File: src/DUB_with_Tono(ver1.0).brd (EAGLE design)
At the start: 100 x 80 mm, 3 parts

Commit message: ベタの追加
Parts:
- removed EDGE1: 10046971-019LF, 10046971-019LF:10046971-019LF
- removed U$2: 5-5530843-4, 5-5530843-4:5-5530843-4
- added DUB: 10046971-019LF, 10046971-019LF:10046971-019LF
- added 遠野: 5-5530843-4, 5-5530843-4:5-5530843-4
- moved U$1 70.8 mm to (45.1, 8.33)
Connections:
- removed net N$1: U$2.P$1, U$2.P$2, U$2.P$3, U$2.P$37, U$2.P$38, U$2.P$39, U$2.P$4, U$2.P$40
- net DIR_IN: now also DUB.P$26, 遠野.P$21; no longer EDGE1.P$26
- net GND: now also DUB.P$28, DUB.P$29, DUB.P$30, DUB.P$31, DUB.P$32, DUB.P$33, DUB.P$34, DUB.P$35, DUB.P$36, DUB.P$37, DUB.P$38, DUB.P$39, 遠野.P$14, 遠野.P$15, 遠野.P$16, 遠野.P$17, 遠野.P$18, 遠野.P$23, 遠野.P$24, 遠野.P$25, 遠野.P$26, 遠野.P$27; no longer EDGE1.P$28, EDGE1.P$29, EDGE1.P$30, EDGE1.P$31, EDGE1.P$32, EDGE1.P$33, EDGE1.P$34, EDGE1.P$35, EDGE1.P$36, EDGE1.P$37, EDGE1.P$38, EDGE1.P$39
- net GND_IN: now also DUB.P$24, 遠野.P$19; no longer EDGE1.P$24
- net PWM_IN: now also DUB.P$25, 遠野.P$20; no longer EDGE1.P$25
- net SA: now also DUB.P$1, DUB.P$2, DUB.P$3, DUB.P$4, DUB.P$45, DUB.P$46, DUB.P$47, DUB.P$48, DUB.P$49, DUB.P$5, DUB.P$50, 遠野.P$1, 遠野.P$2, 遠野.P$3, 遠野.P$37, 遠野.P$38, 遠野.P$39, 遠野.P$4, 遠野.P$40; no longer EDGE1.P$1, EDGE1.P$2, EDGE1.P$3, EDGE1.P$4, EDGE1.P$45, EDGE1.P$46, EDGE1.P$47, EDGE1.P$48, EDGE1.P$49, EDGE1.P$5, EDGE1.P$50
- net SB: now also DUB.P$10, DUB.P$11, DUB.P$40, DUB.P$41, DUB.P$42, DUB.P$43, DUB.P$44, DUB.P$6, DUB.P$7, DUB.P$8, DUB.P$9, 遠野.P$33, 遠野.P$34, 遠野.P$35, 遠野.P$36, 遠野.P$5, 遠野.P$6, 遠野.P$7, 遠野.P$8; no longer EDGE1.P$10, EDGE1.P$11, EDGE1.P$40, EDGE1.P$41, EDGE1.P$42, EDGE1.P$43, EDGE1.P$44, EDGE1.P$6, EDGE1.P$7, EDGE1.P$8, EDGE1.P$9
- net VCC: now also DUB.P$12, DUB.P$13, DUB.P$14, DUB.P$15, DUB.P$16, DUB.P$17, DUB.P$18, DUB.P$19, DUB.P$20, DUB.P$21, DUB.P$22, DUB.P$23, 遠野.P$10, 遠野.P$11, 遠野.P$12, 遠野.P$13, 遠野.P$28, 遠野.P$29, 遠野.P$30, 遠野.P$31, 遠野.P$32, 遠野.P$9; no longer EDGE1.P$12, EDGE1.P$13, EDGE1.P$14, EDGE1.P$15, EDGE1.P$16, EDGE1.P$17, EDGE1.P$18, EDGE1.P$19, EDGE1.P$20, EDGE1.P$21, EDGE1.P$22, EDGE1.P$23
- net VCC_IN: now also DUB.P$27, 遠野.P$22; no longer EDGE1.P$27
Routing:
- net VCC_IN: track 0.00 -> 14.0 mm
- net GND_IN: track 0.00 -> 14.0 mm
- net DIR_IN: track 0.00 -> 14.0 mm
- net PWM_IN: track 0.00 -> 14.0 mm
- added copper zone on layer 1, net GND
- added copper zone on layer 16, net GND
- added copper zone on layer 1, net SA
- added copper zone on layer 16, net SA
- added copper zone on layer 1, net SB
- added copper zone on layer 16, net SB
- added copper zone on layer 1, net VCC
- added copper zone on layer 16, net VCC
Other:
- board size 100 x 80 mm -> 66 x 21.6 mm

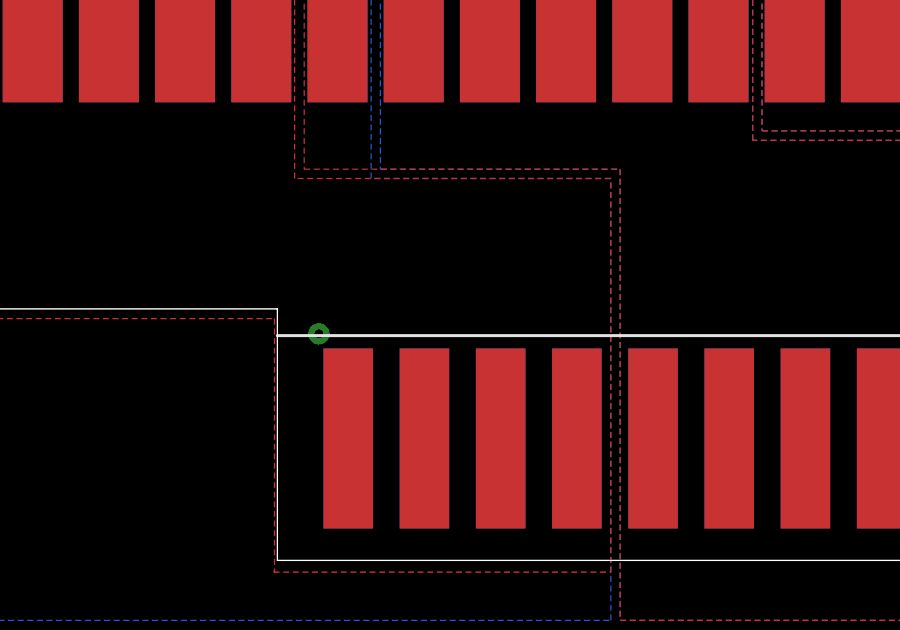
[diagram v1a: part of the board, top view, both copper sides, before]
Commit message: ビアの追加
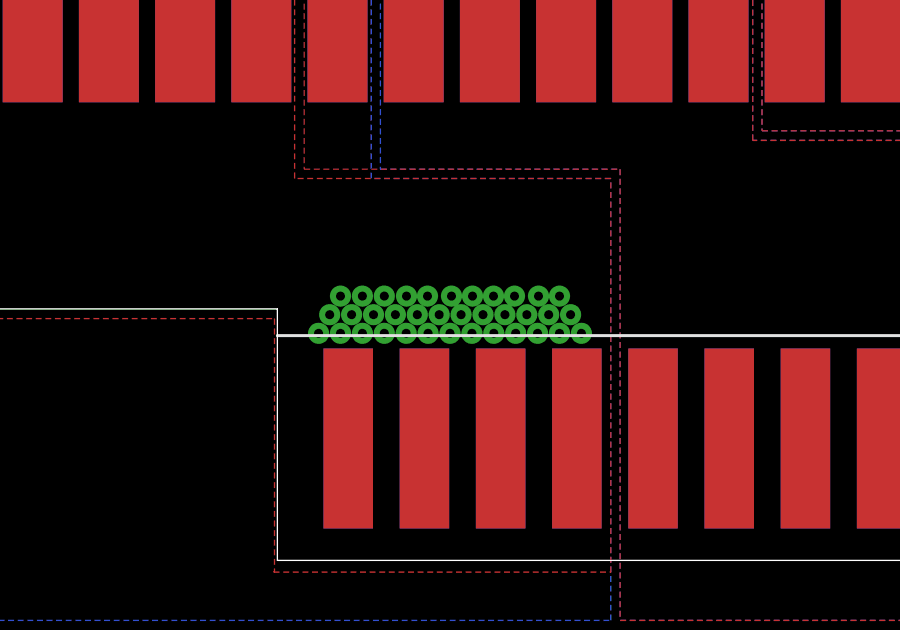
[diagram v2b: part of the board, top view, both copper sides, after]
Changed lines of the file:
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@@
 <setting verticaltext="up"/>
 </settings>
-<grid distance="0.01" unitdist="mm" unit="mm" style="lines" multiple="1" display="no" altdistance="0.01" altunitdist="mm" altunit="mm"/>
+<grid distance="0.1" unitdist="mm" unit="mm" style="lines" multiple="1" display="no" altdistance="0.01" altunitdist="mm" altunit="mm"/>
 <layers>
 <layer number="1" name="Top" color="4" fill="1" visible="yes" active="yes"/>
@@
 <vertex x="13.63" y="21.811109375"/>
 </polygon>
+<via x="14.43" y="7.57" extent="1-16" drill="0.3"/>
+<via x="14.8" y="8.19" extent="1-16" drill="0.3"/>
+<via x="15.16" y="8.81" extent="1-16" drill="0.3"/>
+<via x="15.16" y="7.57" extent="1-16" drill="0.3"/>
+<via x="15.53" y="8.19" extent="1-16" drill="0.3"/>
+<via x="15.89" y="8.81" extent="1-16" drill="0.3"/>
+<via x="15.89" y="7.57" extent="1-16" drill="0.3"/>
+<via x="16.26" y="8.19" extent="1-16" drill="0.3"/>
+<via x="16.62" y="8.81" extent="1-16" drill="0.3"/>
+<via x="16.62" y="7.57" extent="1-16" drill="0.3"/>
+<via x="16.99" y="8.19" extent="1-16" drill="0.3"/>
+<via x="17.36" y="8.81" extent="1-16" drill="0.3"/>
+<via x="17.35" y="7.57" extent="1-16" drill="0.3"/>
+<via x="17.72" y="8.19" extent="1-16" drill="0.3"/>
+<via x="18.06" y="8.81" extent="1-16" drill="0.3"/>
+<via x="18.08" y="7.57" extent="1-16" drill="0.3"/>
+<via x="18.45" y="8.19" extent="1-16" drill="0.3"/>
+<via x="18.86" y="8.81" extent="1-16" drill="0.3"/>
+<via x="18.81" y="7.57" extent="1-16" drill="0.3"/>
+<via x="19.54" y="7.57" extent="1-16" drill="0.3"/>
+<via x="20.27" y="7.57" extent="1-16" drill="0.3"/>
+<via x="21" y="7.57" extent="1-16" drill="0.3"/>
+<via x="21.73" y="7.57" extent="1-16" drill="0.3"/>
+<via x="22.46" y="7.57" extent="1-16" drill="0.3"/>
+<via x="23.19" y="7.57" extent="1-16" drill="0.3"/>
+<via x="19.18" y="8.19" extent="1-16" drill="0.3"/>
+<via x="19.91" y="8.19" extent="1-16" drill="0.3"/>
+<via x="20.64" y="8.19" extent="1-16" drill="0.3"/>
+<via x="21.37" y="8.19" extent="1-16" drill="0.3"/>
+<via x="22.1" y="8.19" extent="1-16" drill="0.3"/>
+<via x="22.83" y="8.19" extent="1-16" drill="0.3"/>
+<via x="19.56" y="8.81" extent="1-16" drill="0.3"/>
+<via x="20.26" y="8.81" extent="1-16" drill="0.3"/>
+<via x="20.96" y="8.81" extent="1-16" drill="0.3"/>
+<via x="21.76" y="8.81" extent="1-16" drill="0.3"/>
+<via x="22.46" y="8.81" extent="1-16" drill="0.3"/>
+<wire x1="12.52" y1="17.92" x2="15.06" y2="17.92" width="0" layer="19" extent="16-16"/>
+<wire x1="12.52" y1="17.92" x2="12.52" y2="17.92" width="0" layer="19" extent="1-16"/>
+<wire x1="9.98" y1="17.92" x2="12.52" y2="17.92" width="0" layer="19" extent="1-16"/>
+<wire x1="9.98" y1="17.92" x2="9.98" y2="17.92" width="0" layer="19" extent="1-16"/>
+<wire x1="7.44" y1="17.92" x2="9.98" y2="17.92" width="0" layer="19" extent="1-1"/>
+<wire x1="7.44" y1="17.92" x2="7.44" y2="17.92" width="0" layer="19" extent="1-16"/>
+<wire x1="4.9" y1="17.92" x2="7.44" y2="17.92" width="0" layer="19" extent="1-1"/>
+<wire x1="4.9" y1="17.92" x2="4.9" y2="17.92" width="0" layer="19" extent="1-16"/>
+<wire x1="2.36" y1="17.92" x2="4.9" y2="17.92" width="0" layer="19" extent="1-1"/>
+<wire x1="2.36" y1="17.92" x2="2.36" y2="17.92" width="0" layer="19" extent="1-16"/>
+<wire x1="15.16" y1="8.81" x2="15.06" y2="17.92" width="0" layer="19" extent="16-16"/>
+<wire x1="15.53" y1="8.19" x2="15.16" y2="8.81" width="0" layer="19" extent="1-1"/>
+<wire x1="15.89" y1="8.81" x2="15.16" y2="8.81" width="0" layer="19" extent="1-1"/>
+<wire x1="16.26" y1="8.19" x2="15.53" y2="8.19" width="0" layer="19" extent="1-1"/>
+<wire x1="16.62" y1="8.81" x2="15.89" y2="8.81" width="0" layer="19" extent="1-1"/>
+<wire x1="16.99" y1="8.19" x2="16.26" y2="8.19" width="0" layer="19" extent="1-1"/>
+<wire x1="17.36" y1="8.81" x2="16.62" y2="8.81" width="0" layer="19" extent="1-1"/>
+<wire x1="18.06" y1="8.81" x2="17.36" y2="8.81" width="0" layer="19" extent="1-1"/>
+<wire x1="17.72" y1="8.19" x2="18.06" y2="8.81" width="0" layer="19" extent="1-1"/>
+<wire x1="18.45" y1="8.19" x2="18.06" y2="8.81" width="0" layer="19" extent="1-1"/>
+<wire x1="19.18" y1="8.19" x2="18.45" y2="8.19" width="0" layer="19" extent="1-1"/>
+<wire x1="18.86" y1="8.81" x2="19.18" y2="8.19" width="0" layer="19" extent="1-1"/>
+<wire x1="19.56" y1="8.81" x2="18.86" y2="8.81" width="0" layer="19" extent="1-1"/>
+<wire x1="19.91" y1="8.19" x2="19.56" y2="8.81" width="0" layer="19" extent="1-1"/>
+<wire x1="20.26" y1="8.81" x2="19.56" y2="8.81" width="0" layer="19" extent="1-1"/>
+<wire x1="20.96" y1="8.81" x2="20.26" y2="8.81" width="0" layer="19" extent="1-1"/>
+<wire x1="20.64" y1="8.19" x2="20.96" y2="8.81" width="0" layer="19" extent="1-1"/>
+<wire x1="21.37" y1="8.19" x2="20.64" y2="8.19" width="0" layer="19" extent="1-1"/>
+<wire x1="22.1" y1="8.19" x2="21.37" y2="8.19" width="0" layer="19" extent="1-1"/>
+<wire x1="21.76" y1="8.81" x2="22.1" y2="8.19" width="0" layer="19" extent="1-1"/>
+<wire x1="22.46" y1="8.81" x2="21.76" y2="8.81" width="0" layer="19" extent="1-1"/>
+<wire x1="22.83" y1="8.19" x2="22.1" y2="8.19" width="0" layer="19" extent="1-1"/>
+<wire x1="23.19" y1="7.57" x2="22.83" y2="8.19" width="0" layer="19" extent="1-1"/>
+<wire x1="21" y1="7.57" x2="20.64" y2="8.19" width="0" layer="19" extent="1-1"/>
+<wire x1="21.73" y1="7.57" x2="21.37" y2="8.19" width="0" layer="19" extent="1-1"/>
+<wire x1="22.46" y1="7.57" x2="22.1" y2="8.19" width="0" layer="19" extent="1-1"/>
+<wire x1="18.08" y1="7.57" x2="17.72" y2="8.19" width="0" layer="19" extent="1-1"/>
+<wire x1="18.81" y1="7.57" x2="18.45" y2="8.19" width="0" layer="19" extent="1-1"/>
+<wire x1="19.54" y1="7.57" x2="19.18" y2="8.19" width="0" layer="19" extent="1-1"/>
+<wire x1="20.27" y1="7.57" x2="19.91" y2="8.19" width="0" layer="19" extent="1-1"/>
+<wire x1="14.8" y1="8.19" x2="15.16" y2="8.81" width="0" layer="19" extent="1-1"/>
+<wire x1="15.89" y1="7.57" x2="15.53" y2="8.19" width="0" layer="19" extent="1-1"/>
+<wire x1="16.62" y1="7.57" x2="16.26" y2="8.19" width="0" layer="19" extent="1-1"/>
+<wire x1="17.35" y1="7.57" x2="16.99" y2="8.19" width="0" layer="19" extent="1-1"/>
+<wire x1="14.43" y1="7.57" x2="14.8" y2="8.19" width="0" layer="19" extent="1-1"/>
+<wire x1="15.16" y1="7.57" x2="15.53" y2="8.19" width="0" layer="19" extent="1-1"/>
+<wire x1="23.0378" y1="4.064" x2="23.19" y2="7.57" width="0" layer="19" extent="1-1"/>
+<wire x1="23.0378" y1="4.064" x2="23.0378" y2="4.064" width="0" layer="19" extent="1-16"/>
+<wire x1="20.4978" y1="4.064" x2="23.0378" y2="4.064" width="0" layer="19" extent="1-1"/>
+<wire x1="20.4978" y1="4.064" x2="20.4978" y2="4.064" width="0" layer="19" extent="1-16"/>
+<wire x1="17.9578" y1="4.064" x2="20.4978" y2="4.064" width="0" layer="19" extent="1-1"/>
+<wire x1="17.9578" y1="4.064" x2="17.9578" y2="4.064" width="0" layer="19" extent="1-16"/>
+<wire x1="15.4178" y1="4.064" x2="17.9578" y2="4.064" width="0" layer="19" extent="1-1"/>
 <wire x1="15.4178" y1="4.064" x2="15.4178" y2="4.064" width="0" layer="19" extent="1-16"/>
 </signal>
@@
 <wire x1="35.7378" y1="4.064" x2="35.7378" y2="4.064" width="0" layer="19" extent="1-16"/>
 </signal>
-<signal name="N$2">
-<via x="14.44" y="7.55" extent="1-16" drill="0.3"/>
-</signal>
 </signals>

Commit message: 前バージョン
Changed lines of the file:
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@@
 <setting verticaltext="up"/>
 </settings>
-<grid distance="0.1" unitdist="mm" unit="mm" style="lines" multiple="1" display="no" altdistance="0.01" altunitdist="mm" altunit="mm"/>
+<grid distance="0.01" unitdist="mm" unit="mm" style="lines" multiple="1" display="no" altdistance="0.01" altunitdist="mm" altunit="mm"/>
 <layers>
 <layer number="1" name="Top" color="4" fill="1" visible="yes" active="yes"/>
@@
 <vertex x="13.63" y="21.811109375"/>
 </polygon>
-<via x="14.43" y="7.57" extent="1-16" drill="0.3"/>
-<via x="14.8" y="8.19" extent="1-16" drill="0.3"/>
-<via x="15.16" y="8.81" extent="1-16" drill="0.3"/>
-<via x="15.16" y="7.57" extent="1-16" drill="0.3"/>
-<via x="15.53" y="8.19" extent="1-16" drill="0.3"/>
-<via x="15.89" y="8.81" extent="1-16" drill="0.3"/>
-<via x="15.89" y="7.57" extent="1-16" drill="0.3"/>
-<via x="16.26" y="8.19" extent="1-16" drill="0.3"/>
-<via x="16.62" y="8.81" extent="1-16" drill="0.3"/>
-<via x="16.62" y="7.57" extent="1-16" drill="0.3"/>
-<via x="16.99" y="8.19" extent="1-16" drill="0.3"/>
-<via x="17.36" y="8.81" extent="1-16" drill="0.3"/>
-<via x="17.35" y="7.57" extent="1-16" drill="0.3"/>
-<via x="17.72" y="8.19" extent="1-16" drill="0.3"/>
-<via x="18.06" y="8.81" extent="1-16" drill="0.3"/>
-<via x="18.08" y="7.57" extent="1-16" drill="0.3"/>
-<via x="18.45" y="8.19" extent="1-16" drill="0.3"/>
-<via x="18.86" y="8.81" extent="1-16" drill="0.3"/>
-<via x="18.81" y="7.57" extent="1-16" drill="0.3"/>
-<via x="19.54" y="7.57" extent="1-16" drill="0.3"/>
-<via x="20.27" y="7.57" extent="1-16" drill="0.3"/>
-<via x="21" y="7.57" extent="1-16" drill="0.3"/>
-<via x="21.73" y="7.57" extent="1-16" drill="0.3"/>
-<via x="22.46" y="7.57" extent="1-16" drill="0.3"/>
-<via x="23.19" y="7.57" extent="1-16" drill="0.3"/>
-<via x="19.18" y="8.19" extent="1-16" drill="0.3"/>
-<via x="19.91" y="8.19" extent="1-16" drill="0.3"/>
-<via x="20.64" y="8.19" extent="1-16" drill="0.3"/>
-<via x="21.37" y="8.19" extent="1-16" drill="0.3"/>
-<via x="22.1" y="8.19" extent="1-16" drill="0.3"/>
-<via x="22.83" y="8.19" extent="1-16" drill="0.3"/>
-<via x="19.56" y="8.81" extent="1-16" drill="0.3"/>
-<via x="20.26" y="8.81" extent="1-16" drill="0.3"/>
-<via x="20.96" y="8.81" extent="1-16" drill="0.3"/>
-<via x="21.76" y="8.81" extent="1-16" drill="0.3"/>
-<via x="22.46" y="8.81" extent="1-16" drill="0.3"/>
-<wire x1="12.52" y1="17.92" x2="15.06" y2="17.92" width="0" layer="19" extent="16-16"/>
-<wire x1="12.52" y1="17.92" x2="12.52" y2="17.92" width="0" layer="19" extent="1-16"/>
-<wire x1="9.98" y1="17.92" x2="12.52" y2="17.92" width="0" layer="19" extent="1-16"/>
-<wire x1="9.98" y1="17.92" x2="9.98" y2="17.92" width="0" layer="19" extent="1-16"/>
-<wire x1="7.44" y1="17.92" x2="9.98" y2="17.92" width="0" layer="19" extent="1-1"/>
-<wire x1="7.44" y1="17.92" x2="7.44" y2="17.92" width="0" layer="19" extent="1-16"/>
-<wire x1="4.9" y1="17.92" x2="7.44" y2="17.92" width="0" layer="19" extent="1-1"/>
-<wire x1="4.9" y1="17.92" x2="4.9" y2="17.92" width="0" layer="19" extent="1-16"/>
-<wire x1="2.36" y1="17.92" x2="4.9" y2="17.92" width="0" layer="19" extent="1-1"/>
-<wire x1="2.36" y1="17.92" x2="2.36" y2="17.92" width="0" layer="19" extent="1-16"/>
-<wire x1="15.16" y1="8.81" x2="15.06" y2="17.92" width="0" layer="19" extent="16-16"/>
-<wire x1="15.53" y1="8.19" x2="15.16" y2="8.81" width="0" layer="19" extent="1-1"/>
-<wire x1="15.89" y1="8.81" x2="15.16" y2="8.81" width="0" layer="19" extent="1-1"/>
-<wire x1="16.26" y1="8.19" x2="15.53" y2="8.19" width="0" layer="19" extent="1-1"/>
-<wire x1="16.62" y1="8.81" x2="15.89" y2="8.81" width="0" layer="19" extent="1-1"/>
-<wire x1="16.99" y1="8.19" x2="16.26" y2="8.19" width="0" layer="19" extent="1-1"/>
-<wire x1="17.36" y1="8.81" x2="16.62" y2="8.81" width="0" layer="19" extent="1-1"/>
-<wire x1="18.06" y1="8.81" x2="17.36" y2="8.81" width="0" layer="19" extent="1-1"/>
-<wire x1="17.72" y1="8.19" x2="18.06" y2="8.81" width="0" layer="19" extent="1-1"/>
-<wire x1="18.45" y1="8.19" x2="18.06" y2="8.81" width="0" layer="19" extent="1-1"/>
-<wire x1="19.18" y1="8.19" x2="18.45" y2="8.19" width="0" layer="19" extent="1-1"/>
-<wire x1="18.86" y1="8.81" x2="19.18" y2="8.19" width="0" layer="19" extent="1-1"/>
-<wire x1="19.56" y1="8.81" x2="18.86" y2="8.81" width="0" layer="19" extent="1-1"/>
-<wire x1="19.91" y1="8.19" x2="19.56" y2="8.81" width="0" layer="19" extent="1-1"/>
-<wire x1="20.26" y1="8.81" x2="19.56" y2="8.81" width="0" layer="19" extent="1-1"/>
-<wire x1="20.96" y1="8.81" x2="20.26" y2="8.81" width="0" layer="19" extent="1-1"/>
-<wire x1="20.64" y1="8.19" x2="20.96" y2="8.81" width="0" layer="19" extent="1-1"/>
-<wire x1="21.37" y1="8.19" x2="20.64" y2="8.19" width="0" layer="19" extent="1-1"/>
-<wire x1="22.1" y1="8.19" x2="21.37" y2="8.19" width="0" layer="19" extent="1-1"/>
-<wire x1="21.76" y1="8.81" x2="22.1" y2="8.19" width="0" layer="19" extent="1-1"/>
-<wire x1="22.46" y1="8.81" x2="21.76" y2="8.81" width="0" layer="19" extent="1-1"/>
-<wire x1="22.83" y1="8.19" x2="22.1" y2="8.19" width="0" layer="19" extent="1-1"/>
-<wire x1="23.19" y1="7.57" x2="22.83" y2="8.19" width="0" layer="19" extent="1-1"/>
-<wire x1="21" y1="7.57" x2="20.64" y2="8.19" width="0" layer="19" extent="1-1"/>
-<wire x1="21.73" y1="7.57" x2="21.37" y2="8.19" width="0" layer="19" extent="1-1"/>
-<wire x1="22.46" y1="7.57" x2="22.1" y2="8.19" width="0" layer="19" extent="1-1"/>
-<wire x1="18.08" y1="7.57" x2="17.72" y2="8.19" width="0" layer="19" extent="1-1"/>
-<wire x1="18.81" y1="7.57" x2="18.45" y2="8.19" width="0" layer="19" extent="1-1"/>
-<wire x1="19.54" y1="7.57" x2="19.18" y2="8.19" width="0" layer="19" extent="1-1"/>
-<wire x1="20.27" y1="7.57" x2="19.91" y2="8.19" width="0" layer="19" extent="1-1"/>
-<wire x1="14.8" y1="8.19" x2="15.16" y2="8.81" width="0" layer="19" extent="1-1"/>
-<wire x1="15.89" y1="7.57" x2="15.53" y2="8.19" width="0" layer="19" extent="1-1"/>
-<wire x1="16.62" y1="7.57" x2="16.26" y2="8.19" width="0" layer="19" extent="1-1"/>
-<wire x1="17.35" y1="7.57" x2="16.99" y2="8.19" width="0" layer="19" extent="1-1"/>
-<wire x1="14.43" y1="7.57" x2="14.8" y2="8.19" width="0" layer="19" extent="1-1"/>
-<wire x1="15.16" y1="7.57" x2="15.53" y2="8.19" width="0" layer="19" extent="1-1"/>
-<wire x1="23.0378" y1="4.064" x2="23.19" y2="7.57" width="0" layer="19" extent="1-1"/>
-<wire x1="23.0378" y1="4.064" x2="23.0378" y2="4.064" width="0" layer="19" extent="1-16"/>
-<wire x1="20.4978" y1="4.064" x2="23.0378" y2="4.064" width="0" layer="19" extent="1-1"/>
-<wire x1="20.4978" y1="4.064" x2="20.4978" y2="4.064" width="0" layer="19" extent="1-16"/>
-<wire x1="17.9578" y1="4.064" x2="20.4978" y2="4.064" width="0" layer="19" extent="1-1"/>
-<wire x1="17.9578" y1="4.064" x2="17.9578" y2="4.064" width="0" layer="19" extent="1-16"/>
-<wire x1="15.4178" y1="4.064" x2="17.9578" y2="4.064" width="0" layer="19" extent="1-1"/>
 <wire x1="15.4178" y1="4.064" x2="15.4178" y2="4.064" width="0" layer="19" extent="1-16"/>
 </signal>
@@
 <vertex x="16.49" y="24"/>
 <vertex x="16.49" y="13.04"/>
-<vertex x="24.48" y="13.04"/>
-<vertex x="24.48" y="-2"/>
+<vertex x="25.91" y="13.04"/>
+<vertex x="25.91" y="-2"/>
 <vertex x="34.17" y="-2"/>
 <vertex x="34.17" y="14"/>
@@
 <wire x1="35.7378" y1="4.064" x2="35.7378" y2="4.064" width="0" layer="19" extent="1-16"/>
 </signal>
+<signal name="N$2">
+<via x="14.44" y="7.55" extent="1-16" drill="0.3"/>
+</signal>
 </signals>
